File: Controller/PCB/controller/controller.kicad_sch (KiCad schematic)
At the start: 80 parts, among them J1 nRF24L01_Conn, J2 SERIAL_DEBUG_Conn, Q1 S9013, Q2 S9013, Q3 S9013, Q4 S9013, Q5 S9013, Q6 S9013, SW1 SW_SPDT, SW2 SW_SPDT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

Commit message: Continue updating Hardware
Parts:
- removed Btn_4: SW_SPST, Button_Switch_SMD:SW_Push_1P1T_NO_6x6mm_H9.5mm, symbol Switch:SW_SPST
- removed C1, C2: 100nF, Capacitor_SMD:C_0603_1608Metric, symbol Device:C
- removed D2, D8: BLUE, LED_SMD:LED_0603_1608Metric, symbol Device:LED
- removed D3: GREEN, LED_SMD:LED_0603_1608Metric, symbol Device:LED
- removed D9: RED, LED_SMD:LED_0603_1608Metric, symbol Device:LED
- removed J2: SERIAL_DEBUG_Conn, Connector_PinHeader_2.54mm:PinHeader_2x04_P2.54mm_Vertical_SMD, symbol Connector_Generic:Conn_02x04_Odd_Even
- removed POT_1, POT_2: R_POT, My_library:PDB12 Series, symbol Device:R_POT
- removed Q3, Q5, Q6: S9013, Package_TO_SOT_SMD:SOT-23, symbol Transistor_BJT:2N2219
- removed R17, R22, R35: 1K, Resistor_SMD:R_0603_1608Metric, symbol Device:R
- removed R18, R20, R23: 10K, Resistor_SMD:R_0603_1608Metric, symbol Device:R
- removed R25, R33: 390R, Resistor_SMD:R_0603_1608Metric, symbol Device:R
- removed R27: 2K, Resistor_SMD:R_0603_1608Metric, symbol Device:R
- removed R32, R34: 4K7, Resistor_SMD:R_0603_1608Metric, symbol Device:R
- removed R7, R8: 620, Resistor_SMD:R_0603_1608Metric, symbol Device:R
- removed SW2: SW_SPDT, symbol Switch:SW_SPDT
- removed U3, U4: NLAS4684, My_library:NLAS4684, symbol My_Library.lib:NLAS4684
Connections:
- net Btn_4: no longer names the net of A1.8 (D5)
- net SERIAL_IRQ: no longer names the net of A1.11 (D8)
- net SW_2: no longer names the net of A1.10 (D7)
- no-connect marks 9 -> 8
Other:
- moved on the sheet: A1, Btn_3, R14, R16, R19, R21, SW1

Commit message: Finalise Circuit Schematic
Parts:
- added C1, C11: 10uF, Capacitor_SMD:CP_Elec_4x5.4, symbol Device:C
- added C12, C13, C2: 100nF, Capacitor_SMD:C_0603_1608Metric, symbol Device:C
- added D2: 1N5817, My_library:1N5817M, symbol Diode:1N5817
- added U3: LM2940-3.0, Package_TO_SOT_SMD:SOT-223, symbol Regulator_Linear:LM1117-5.0
- BZ1: footprint Buzzer_Beeper:Buzzer_12x9.5RM7.6 -> My_library:Buzzer
- C10, C9: footprint (none) -> Capacitor_SMD:CP_Elec_4x5.4
- SW1: footprint (none) -> My_library:KNX-1-D1
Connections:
- net LED_2 is gone; now on net Btn_1: A1.1 (D1/TX)
- net POT_1 is gone; now on net Btn_3: A1.21 (A2)
- net POT_2 is gone; now on net R_PITCH: A1.22 (A3)
- net +3V3: now also C1.1, C11.1, C12.1, C13.2, U3.2 (VO)
- net +BATT: now also C2.1, D2.1 (K), U3.3 (VI)
- net BUZZER: now also A1.8 (D5); no longer A1.20 (A1)
- net Btn_1: no longer A1.5 (D2)
- net Btn_2: now also A1.9 (D6); no longer A1.6 (D3)
- net Btn_3: no longer A1.7 (D4)
- net Earth: now also C1.2, C11.2, C12.2, C13.1, C2.2, D2.2 (A), U3.1 (GND)
- net L_PITCH: now also A1.19 (A0); no longer A1.26 (A7)
- net L_ROLL: now also A1.20 (A1); no longer A1.25 (A6)
- net NRF_CE: now also A1.14 (D11); no longer A1.12 (D9)
- net NRF_CSN: now also A1.15 (D12); no longer A1.16 (D13)
- net NRF_IRQ: now also A1.12 (D9)
- net NRF_SCK: now also A1.16 (D13); no longer A1.13 (D10)
- net RESET: now also A1.3 (~{RESET}); no longer A1.28 (~{RESET})
- net R_PITCH: no longer A1.24 (A5)
- net SERIAL_MISO: now also A1.13 (D10); no longer A1.15 (D12)
- net SERIAL_MOSI: now also A1.5 (D2); no longer A1.14 (D11)
- net SW_1: now also A1.6 (D3); no longer A1.9 (D6)
- no-connect marks 8 -> 14
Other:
- company: (none) -> Luke W
- title: (none) -> Project ORCA Controller
- moved on the sheet: A1, C3, C4, C5, C6, J1, R2, R3, R4, R5, U1, U2

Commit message: Add power switch
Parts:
- added PWR_SW: SW_SPDT, My_library:KNX-1-D1, symbol Switch:SW_SPDT
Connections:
- net +BATT: now also PWR_SW.1 (A); no longer C2.1, C7.1, D2.1 (K), D6.1 (K), U3.3 (VI), U5.3 (VI)
- new net BAT_PWR: C2.1, C7.1, D2.1 (K), D6.1 (K), PWR_SW.2 (B), U3.3 (VI), U5.3 (VI)
- no-connect marks 14 -> 15
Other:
- moved on the sheet: C1, C10, C11, C13, C2, C7, C8, C9, D2, D6, U3, U5

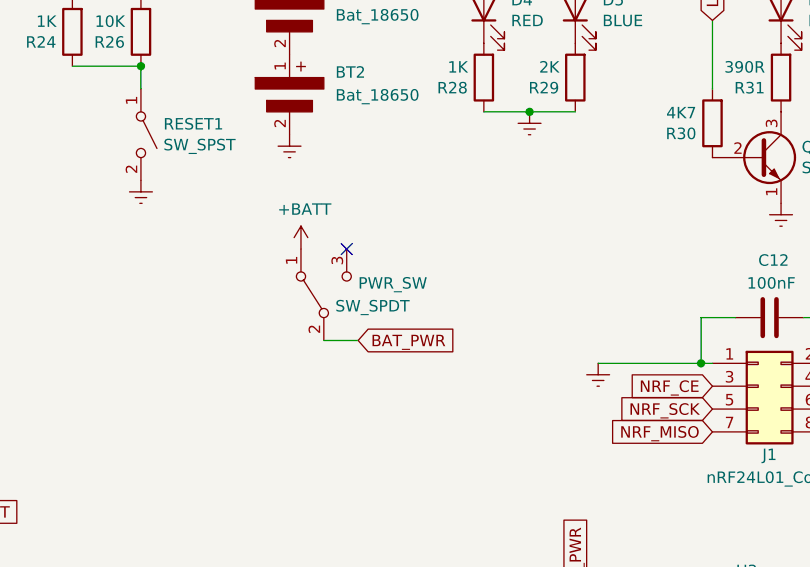
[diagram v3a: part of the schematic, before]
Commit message: Rename power switch
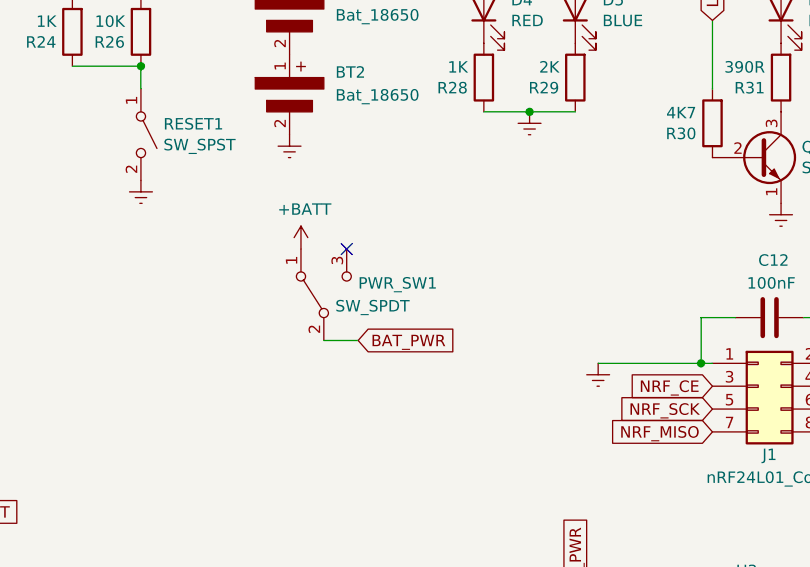
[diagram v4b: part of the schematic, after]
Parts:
- renumbered PWR_SW to PWR_SW1
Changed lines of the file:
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@@
   (symbol (lib_id "Switch:SW_SPDT") (at 204.47 54.61 90) (unit 1)
     (in_bom yes) (on_board yes)
-    (property "Reference" "PWR_SW" (id 0) (at 208.28 53.34 90)
+    (property "Reference" "PWR_SW1" (id 0) (at 208.28 53.34 90)
       (effects (font (size 1.27 1.27)) (justify right))
     )
@@
     )
     (path "/50647faf-6aa6-4c67-a804-7f8cfafef24c"
-      (reference "PWR_SW") (unit 1) (value "SW_SPDT") (footprint "My_library:KNX-1-D1")
+      (reference "PWR_SW1") (unit 1) (value "SW_SPDT") (footprint "My_library:KNX-1-D1")
     )
     (path "/00000000-0000-0000-0000-000062073873"

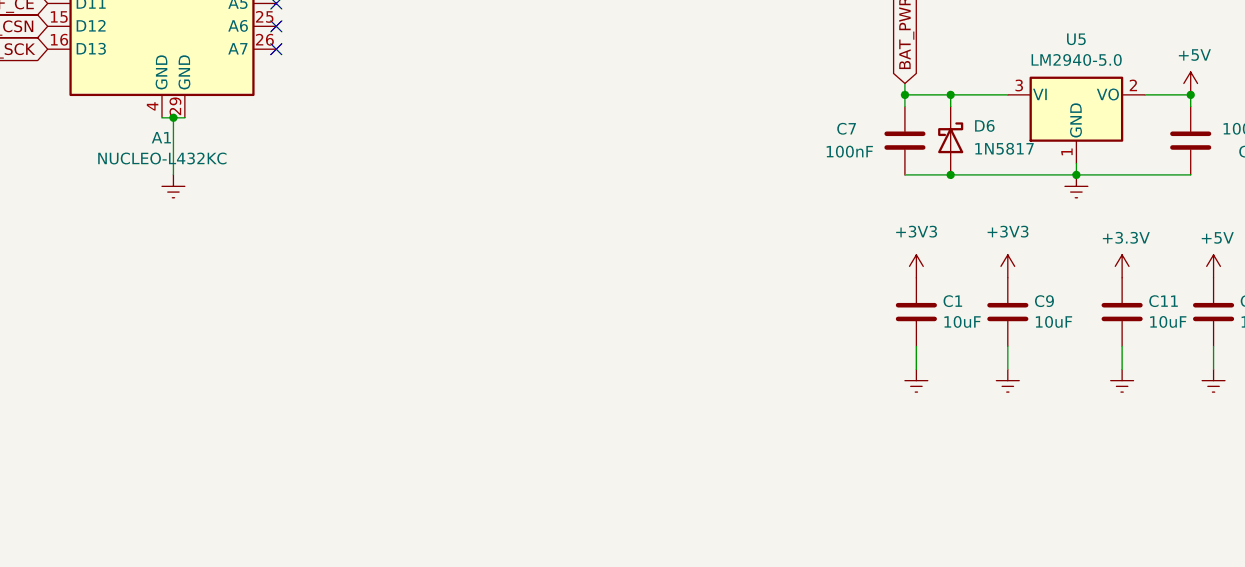
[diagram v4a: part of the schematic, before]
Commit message: Place Components on the PCB
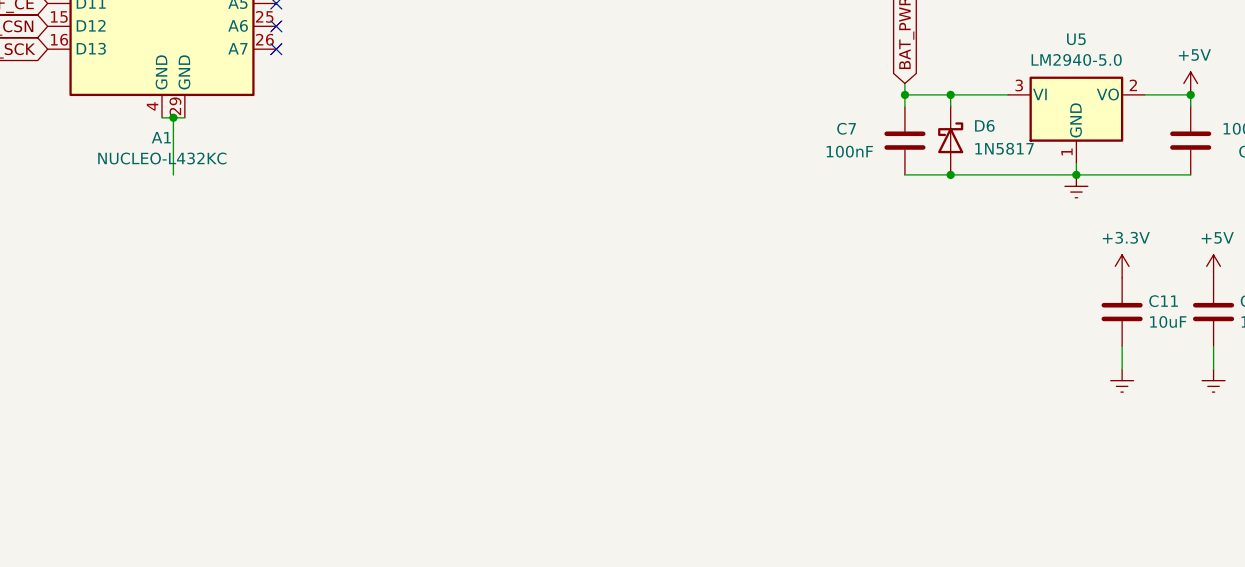
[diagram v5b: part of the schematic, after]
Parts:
- removed C1, C9: 10uF, Capacitor_SMD:CP_Elec_4x5.4, symbol Device:C
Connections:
- net Earth: no longer A1.29 (GND), A1.4 (GND)
- new net: A1.29 (GND), A1.4 (GND)
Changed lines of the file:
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@@
-    (stroke (width 0) (type default) (color 0 0 0 0))
-  )
-  (wire (pts (xy 233.68 142.24) (xy 233.68 144.78))
     (stroke (width 0) (type default) (color 0 0 0 0))
   )
   (wire (pts (xy 57.15 33.02) (xy 59.69 33.02))
-    (stroke (width 0) (type default) (color 0 0 0 0))
-  )
-  (wire (pts (xy 243.84 142.24) (xy 243.84 144.78))
     (stroke (width 0) (type default) (color 0 0 0 0))
   )
@@
     )
     (property "Datasheet" "~" (id 3) (at 234.95 62.23 0)
-      (effects (font (size 1.27 1.27)) hide)
-    )
-    (pin "1")
-  )
-  (symbol (lib_id "Device:C") (at 243.84 138.43 0) (unit 1)
-    (in_bom yes) (on_board yes)
-    (property "Reference" "C9" (id 0) (at 246.761 137.2616 0)
-      (effects (font (size 1.27 1.27)) (justify left))
-    )
-    (property "Value" "10uF" (id 1) (at 246.761 139.573 0)
-      (effects (font (size 1.27 1.27)) (justify left))
-    )
-    (property "Footprint" "Capacitor_SMD:CP_Elec_4x5.4" (id 2) (at 244.8052 142.24 0)
-      (effects (font (size 1.27 1.27)) hide)
-    )
-    (property "Datasheet" "~" (id 3) (at 243.84 138.43 0)
-      (effects (font (size 1.27 1.27)) hide)
-    )
-    (pin "1")
-    (pin "2")
-  )
-  (symbol (lib_id "power:Earth") (at 243.84 144.78 0) (unit 1)
-    (in_bom yes) (on_board yes)
-    (property "Reference" "#PWR0140" (id 0) (at 243.84 151.13 0)
-      (effects (font (size 1.27 1.27)) hide)
-    )
-    (property "Value" "Earth" (id 1) (at 243.84 148.59 0)
-      (effects (font (size 1.27 1.27)) hide)
-    )
-    (property "Footprint" "" (id 2) (at 243.84 144.78 0)
-      (effects (font (size 1.27 1.27)) hide)
-    )
-    (property "Datasheet" "~" (id 3) (at 243.84 144.78 0)
       (effects (font (size 1.27 1.27)) hide)
     )
@@
     (pin "2")
   )
-  (symbol (lib_id "Device:C") (at 233.68 138.43 0) (unit 1)
-    (in_bom yes) (on_board yes)
-    (property "Reference" "C1" (id 0) (at 236.601 137.2616 0)
-      (effects (font (size 1.27 1.27)) (justify left))
-    )
-    (property "Value" "10uF" (id 1) (at 236.601 139.573 0)
-      (effects (font (size 1.27 1.27)) (justify left))
-    )
-    (property "Footprint" "Capacitor_SMD:CP_Elec_4x5.4" (id 2) (at 234.6452 142.24 0)
-      (effects (font (size 1.27 1.27)) hide)
-    )
-    (property "Datasheet" "~" (id 3) (at 233.68 138.43 0)
-      (effects (font (size 1.27 1.27)) hide)
-    )
-    (pin "1")
-    (pin "2")
-  )
-  (symbol (lib_id "power:Earth") (at 233.68 144.78 0) (unit 1)
-    (in_bom yes) (on_board yes)
-    (property "Reference" "#PWR0107" (id 0) (at 233.68 151.13 0)
-      (effects (font (size 1.27 1.27)) hide)
-    )
-    (property "Value" "Earth" (id 1) (at 233.68 148.59 0)
-      (effects (font (size 1.27 1.27)) hide)
-    )
-    (property "Footprint" "" (id 2) (at 233.68 144.78 0)
-      (effects (font (size 1.27 1.27)) hide)
-    )
-    (property "Datasheet" "~" (id 3) (at 233.68 144.78 0)
-      (effects (font (size 1.27 1.27)) hide)
-    )
-    (pin "1")
-  )
-  (symbol (lib_id "power:+3V3") (at 243.84 134.62 0) (unit 1)
-    (in_bom yes) (on_board yes) (fields_autoplaced)
-    (property "Reference" "#PWR0109" (id 0) (at 243.84 138.43 0)
-      (effects (font (size 1.27 1.27)) hide)
-    )
-    (property "Value" "+3V3" (id 1) (at 243.84 129.54 0))
-    (property "Footprint" "" (id 2) (at 243.84 134.62 0)
-      (effects (font (size 1.27 1.27)) hide)
-    )
-    (property "Datasheet" "" (id 3) (at 243.84 134.62 0)
-      (effects (font (size 1.27 1.27)) hide)
-    )
-    (pin "1")
-  )
-  (symbol (lib_id "power:Earth") (at 151.13 123.19 0) (unit 1)
-    (in_bom yes) (on_board yes)
-    (property "Reference" "#PWR0122" (id 0) (at 151.13 129.54 0)
-      (effects (font (size 1.27 1.27)) hide)
-    )
-    (property "Value" "Earth" (id 1) (at 151.13 127 0)
-      (effects (font (size 1.27 1.27)) hide)
-    )
-    (property "Footprint" "" (id 2) (at 151.13 123.19 0)
-      (effects (font (size 1.27 1.27)) hide)
-    )
-    (property "Datasheet" "~" (id 3) (at 151.13 123.19 0)
-      (effects (font (size 1.27 1.27)) hide)
-    )
-    (pin "1")
-  )
   (symbol (lib_id "Diode:1N5817") (at 237.49 119.38 270) (unit 1)
     (in_bom yes) (on_board yes) (fields_autoplaced)
@@
     (pin "1")
     (pin "2")
-  )
-  (symbol (lib_id "power:+3V3") (at 233.68 134.62 0) (unit 1)
-    (in_bom yes) (on_board yes) (fields_autoplaced)
-    (property "Reference" "#PWR0108" (id 0) (at 233.68 138.43 0)
-      (effects (font (size 1.27 1.27)) hide)
-    )
-    (property "Value" "+3V3" (id 1) (at 233.68 129.54 0))
-    (property "Footprint" "" (id 2) (at 233.68 134.62 0)
-      (effects (font (size 1.27 1.27)) hide)
-    )
-    (property "Datasheet" "" (id 3) (at 233.68 134.62 0)
-      (effects (font (size 1.27 1.27)) hide)
-    )
-    (pin "1")
   )
   (symbol (lib_id "Device:R") (at 30.48 149.86 270) (unit 1)
@@
       (reference "#PWR0106") (unit 1) (value "+3V3") (footprint "")
     )
-    (path "/187922ea-783f-487a-b578-952ed29e924b"
-      (reference "#PWR0107") (unit 1) (value "Earth") (footprint "")
-    )
-    (path "/3a99a77e-03c7-4f93-beb9-4edcf16cc8b5"
-      (reference "#PWR0108") (unit 1) (value "+3V3") (footprint "")
-    )
-    (path "/194fa176-af2b-4df8-9f80-00a22bdf2c85"
-      (reference "#PWR0109") (unit 1) (value "+3V3") (footprint "")
-    )
     (path "/00000000-0000-0000-0000-000062091695"
       (reference "#PWR0110") (unit 1) (value "+5V") (footprint "")
@@
       (reference "#PWR0121") (unit 1) (value "Earth") (footprint "")
     )
-    (path "/1a9036cd-6ac6-4b59-9217-86bff87821f1"
-      (reference "#PWR0122") (unit 1) (value "Earth") (footprint "")
-    )
     (path "/00000000-0000-0000-0000-00006208d21d"
       (reference "#PWR0123") (unit 1) (value "+5V") (footprint "")
@@
       (reference "#PWR0135") (unit 1) (value "Earth") (footprint "")
     )
-    (path "/00000000-0000-0000-0000-0000620f67b9"
-      (reference "#PWR0140") (unit 1) (value "Earth") (footprint "")
-    )
     (path "/00000000-0000-0000-0000-0000620abc71"
       (reference "#PWR0141") (unit 1) (value "+5V") (footprint "")
@@
       (reference "Btn_3") (unit 1) (value "SW_SPST") (footprint "Button_Switch_SMD:SW_Push_1P1T_NO_6x6mm_H9.5mm")
     )
-    (path "/173368f8-5e28-4094-9454-bbee324b1ee7"
-      (reference "C1") (unit 1) (value "10uF") (footprint "Capacitor_SMD:CP_Elec_4x5.4")
-    )
     (path "/0677ea8d-27ac-4a38-a5c6-9d3125b863f5"
       (reference "C2") (unit 1) (value "100nF") (footprint "Capacitor_SMD:C_0603_1608Metric")
@@
       (reference "C8") (unit 1) (value "100nF") (footprint "Capacitor_SMD:C_0603_1608Metric")
     )
-    (path "/00000000-0000-0000-0000-0000620f58b9"
-      (reference "C9") (unit 1) (value "10uF") (footprint "Capacitor_SMD:CP_Elec_4x5.4")
-    )
     (path "/67491da7-36cd-4ad9-af70-6e64ae182862"

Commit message: Finalise PCB Schematic
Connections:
- net SERIAL_MISO is gone; now on net NRF_MISO: A1.13 (D10)
- net SERIAL_MOSI is gone; now on net NRF_MOSI: A1.5 (D2)
- net Earth: now also A1.29 (GND), A1.4 (GND)
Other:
- moved on the sheet: U1, U2
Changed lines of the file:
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@@
     )
   )
-  (global_label "SERIAL_MOSI" (shape input) (at 137.16 81.28 180) (fields_autoplaced)
+  (global_label "NRF_MOSI" (shape input) (at 137.16 81.28 180) (fields_autoplaced)
     (effects (font (size 1.27 1.27)) (justify right))
-    (property "Intersheet References" "${INTERSHEET_REFS}" (id 0) (at 122.922 81.3594 0)
+    (property "Intersheet References" "${INTERSHEET_REFS}" (id 0) (at 125.5829 81.2006 0)
       (effects (font (size 1.27 1.27)) (justify right) hide)
     )
@@
     )
   )
-  (global_label "SERIAL_MISO" (shape input) (at 137.16 101.6 180) (fields_autoplaced)
+  (global_label "NRF_MISO" (shape input) (at 137.16 101.6 180) (fields_autoplaced)
     (effects (font (size 1.27 1.27)) (justify right))
-    (property "Intersheet References" "${INTERSHEET_REFS}" (id 0) (at 122.922 101.6794 0)
+    (property "Intersheet References" "${INTERSHEET_REFS}" (id 0) (at 125.5829 101.5206 0)
       (effects (font (size 1.27 1.27)) (justify right) hide)
     )
@@
     )
     (property "Datasheet" "~" (id 3) (at 227.33 34.29 0)
-      (effects (font (size 1.27 1.27)) hide)
-    )
-    (pin "1")
-  )
-  (symbol (lib_id "power:Earth") (at 49.53 118.11 0) (unit 1)
-    (in_bom yes) (on_board yes)
-    (property "Reference" "#PWR0119" (id 0) (at 49.53 124.46 0)
-      (effects (font (size 1.27 1.27)) hide)
-    )
-    (property "Value" "Earth" (id 1) (at 49.53 121.92 0)
-      (effects (font (size 1.27 1.27)) hide)
-    )
-    (property "Footprint" "" (id 2) (at 49.53 118.11 0)
-      (effects (font (size 1.27 1.27)) hide)
-    )
-    (property "Datasheet" "~" (id 3) (at 49.53 118.11 0)
       (effects (font (size 1.27 1.27)) hide)
     )
@@
     (pin "1")
   )
-  (symbol (lib_id "power:Earth") (at 49.53 160.02 0) (unit 1)
-    (in_bom yes) (on_board yes)
-    (property "Reference" "#PWR0121" (id 0) (at 49.53 166.37 0)
-      (effects (font (size 1.27 1.27)) hide)
-    )
-    (property "Value" "Earth" (id 1) (at 49.53 163.83 0)
-      (effects (font (size 1.27 1.27)) hide)
-    )
-    (property "Footprint" "" (id 2) (at 49.53 160.02 0)
-      (effects (font (size 1.27 1.27)) hide)
-    )
-    (property "Datasheet" "~" (id 3) (at 49.53 160.02 0)
-      (effects (font (size 1.27 1.27)) hide)
-    )
-    (pin "1")
-  )
   (symbol (lib_id "Device:C") (at 232.41 96.52 0) (unit 1)
     (in_bom yes) (on_board yes)
@@
       (effects (font (size 1.27 1.27)) hide)
     )
-    (pin "GND")
+    (pin "EARTH")
     (pin "SW1")
     (pin "SW2")
@@
     (pin "Y3")
   )
+  (symbol (lib_id "power:Earth") (at 49.53 160.02 0) (unit 1)
+    (in_bom yes) (on_board yes)
+    (property "Reference" "#PWR0109" (id 0) (at 49.53 166.37 0)
+      (effects (font (size 1.27 1.27)) hide)
+    )
+    (property "Value" "Earth" (id 1) (at 49.53 163.83 0)
+      (effects (font (size 1.27 1.27)) hide)
+    )
+    (property "Footprint" "" (id 2) (at 49.53 160.02 0)
+      (effects (font (size 1.27 1.27)) hide)
+    )
+    (property "Datasheet" "~" (id 3) (at 49.53 160.02 0)
+      (effects (font (size 1.27 1.27)) hide)
+    )
+    (pin "1")
+  )
   (symbol (lib_id "Device:R") (at 255.27 30.48 180) (unit 1)
     (in_bom yes) (on_board yes)
@@
     (pin "2")
   )
+  (symbol (lib_id "power:Earth") (at 49.53 118.11 0) (unit 1)
+    (in_bom yes) (on_board yes)
+    (property "Reference" "#PWR0108" (id 0) (at 49.53 124.46 0)
+      (effects (font (size 1.27 1.27)) hide)
+    )
+    (property "Value" "Earth" (id 1) (at 49.53 121.92 0)
+      (effects (font (size 1.27 1.27)) hide)
+    )
+    (property "Footprint" "" (id 2) (at 49.53 118.11 0)
+      (effects (font (size 1.27 1.27)) hide)
+    )
+    (property "Datasheet" "~" (id 3) (at 49.53 118.11 0)
+      (effects (font (size 1.27 1.27)) hide)
+    )
+    (pin "1")
+  )
   (symbol (lib_id "power:+3V3") (at 264.16 91.44 0) (unit 1)
     (in_bom yes) (on_board yes) (fields_autoplaced)
@@
     (pin "1")
   )
-  (symbol (lib_id "My_Library.lib:Joystick") (at 68.58 91.44 0) (unit 1)
+  (symbol (lib_name "Joystick_1") (lib_id "My_Library.lib:Joystick") (at 68.58 91.44 0) (unit 1)
     (in_bom yes) (on_board yes) (fields_autoplaced)
     (property "Reference" "U1" (id 0) (at 82.55 107.9499 0)
@@
       (effects (font (size 1.27 1.27)) hide)
     )
-    (pin "GND")
+    (pin "EARTH")
     (pin "SW1")
     (pin "SW2")
@@
     (pin "1")
   )
+  (symbol (lib_id "power:Earth") (at 151.13 123.19 0) (unit 1)
+    (in_bom yes) (on_board yes)
+    (property "Reference" "#PWR0107" (id 0) (at 151.13 129.54 0)
+      (effects (font (size 1.27 1.27)) hide)
+    )
+    (property "Value" "Earth" (id 1) (at 151.13 127 0)
+      (effects (font (size 1.27 1.27)) hide)
+    )
+    (property "Footprint" "" (id 2) (at 151.13 123.19 0)
+      (effects (font (size 1.27 1.27)) hide)
+    )
+    (property "Datasheet" "~" (id 3) (at 151.13 123.19 0)
+      (effects (font (size 1.27 1.27)) hide)
+    )
+    (pin "1")
+  )
   (symbol (lib_id "power:+5V") (at 134.62 21.59 0) (unit 1)
     (in_bom yes) (on_board yes)
@@
       (reference "#PWR0106") (unit 1) (value "+3V3") (footprint "")
     )
+    (path "/cf0e5c8d-d240-4bfd-ba56-382204e80108"
+      (reference "#PWR0107") (unit 1) (value "Earth") (footprint "")
+    )
+    (path "/86793ad8-5190-41f4-84dc-de6aef1e1b27"
+      (reference "#PWR0108") (unit 1) (value "Earth") (footprint "")
+    )
+    (path "/6d621d9d-b84f-4438-bde4-2df8c0a2b214"
+      (reference "#PWR0109") (unit 1) (value "Earth") (footprint "")
+    )
     (path "/00000000-0000-0000-0000-000062091695"
       (reference "#PWR0110") (unit 1) (value "+5V") (footprint "")
@@
       (reference "#PWR0118") (unit 1) (value "+3.3V") (footprint "")
     )
-    (path "/00000000-0000-0000-0000-00006211ba50"
-      (reference "#PWR0119") (unit 1) (value "Earth") (footprint "")
-    )
     (path "/00000000-0000-0000-0000-00006213857b"
       (reference "#PWR0120") (unit 1) (value "+3.3V") (footprint "")
     )
-    (path "/00000000-0000-0000-0000-000062138597"
-      (reference "#PWR0121") (unit 1) (value "Earth") (footprint "")
-    )
     (path "/00000000-0000-0000-0000-00006208d21d"
